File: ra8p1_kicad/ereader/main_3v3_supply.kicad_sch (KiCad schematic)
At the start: 24 parts, among them Q3 DMN2056U-7, U13 LTC3119IUFD#PBF, U16 74LVC1G17GW,125

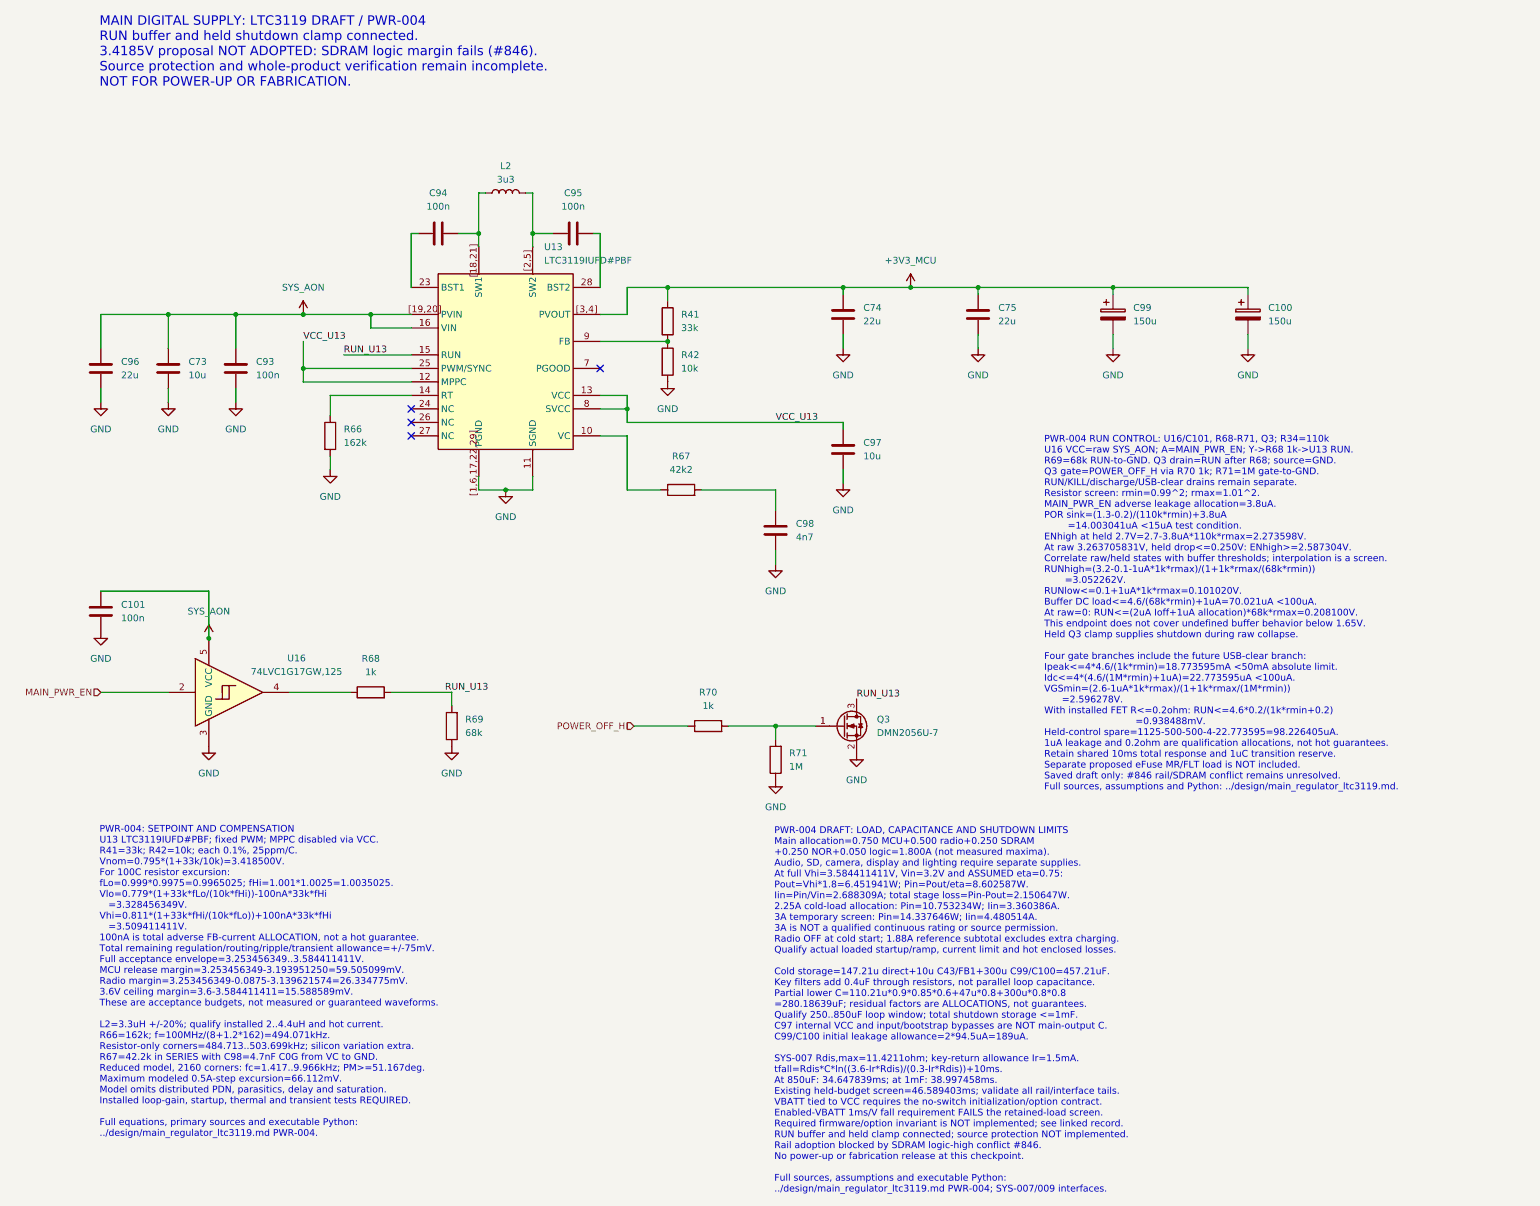
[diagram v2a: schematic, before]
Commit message: Migrate main digital supply to TPS63806 with audited calculations
Replace the LTC3119 stage in native KiCad, refresh sourced passives and linked PWR-006 calculations, and publish the full PDF and BOM. Preserve held enable control and unrelated connectivity. Reset coordination, source protection and physical qualification remain open under #825 and #846.
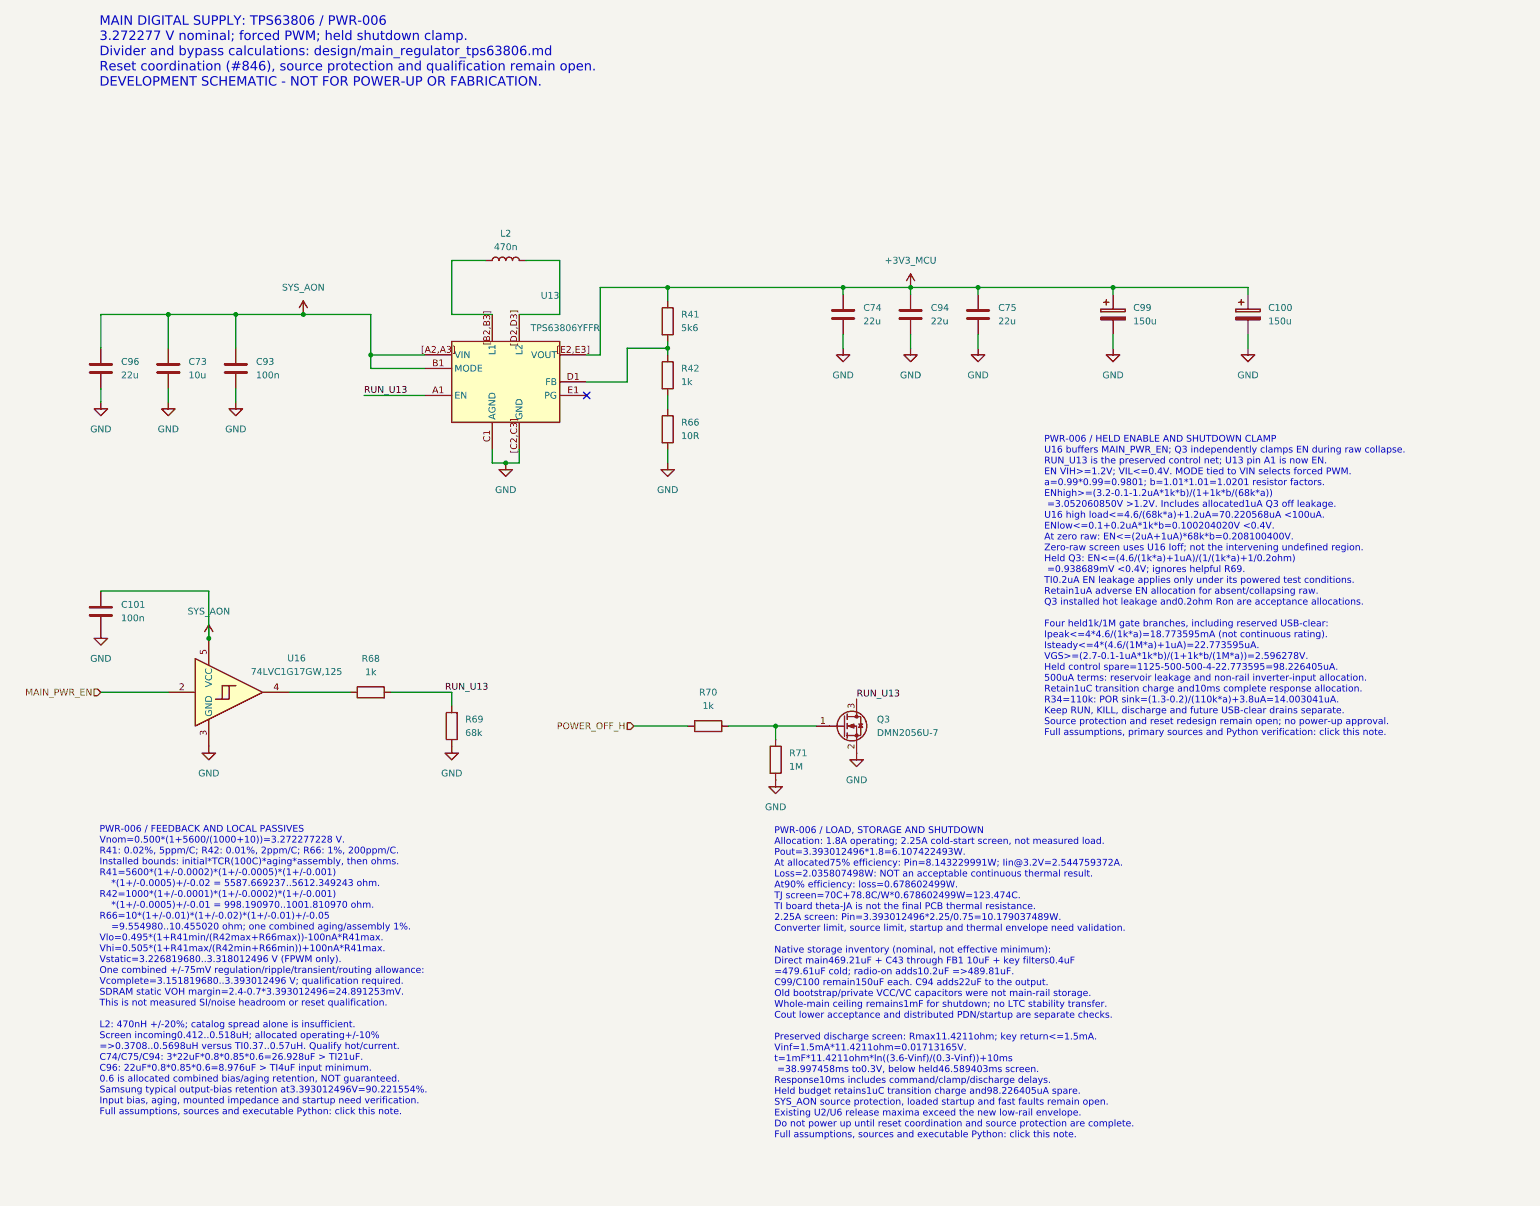
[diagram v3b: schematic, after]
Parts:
- removed C95: 100n, symbol Device:C
- removed C97: 10u, symbol Device:C
- removed C98: 4n7, symbol Device:C
- removed R67: 42k2, symbol Device:R
- removed U13: LTC3119IUFD#PBF, symbol Power_Devices:LTC3119IUFD#PBF
- added U13: TPS63806YFFR, symbol Power_Devices:TPS63806YFFR
- C74, C75: DigiKey_Part_Number 490-5890-1-ND -> 1276-3395-1-ND; DigiKey_URL https://www.digikey.com/en/products/detail/murata-electroni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 -> https://www.digikey.com/en/products/detail/samsung-electro-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; Manufacturer_Name Murata Electronics -> Samsung Electro-Mechanics; Manufacturer_Part_Number GRM32ER71C226KEA8L -> CL32B226MOJNNNE; Procurement_Status Sourced candidate; electrical qualification pending; footpr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 -> Selected; effective capacitance qualification required; foo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; Selection_Basis PWR-004: one of two retained 22uF 16V X7R 10% output cerami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 -> PWR-006: 22uF 20% 16V X7R 1210. C74/C75/C94 output; C96 inp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; Sourcing_Snapshot 2026-09-08; DigiKey stock 30854; USD qty1 0.88000; qty10 0.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 -> 2026-09-08 DigiKey: 162775 stock; USD 0.52/0.318/0.2122 at 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
- C93: Selection_Basis PWR-004: local 100nF VIN16-to-GND bypass; retain short loca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 -> PWR-006: local 100nF VIN A2/A3-to-GND bypass; not main-outp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
- C94: value 100n -> 22u; DigiKey_Part_Number 445-1314-1-ND -> 1276-3395-1-ND; DigiKey_URL https://www.digikey.com/en/products/detail/tdk-corporation/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 -> https://www.digikey.com/en/products/detail/samsung-electro-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; Manufacturer_Name TDK -> Samsung Electro-Mechanics; Manufacturer_Part_Number C1608X7R1H104K080AA -> CL32B226MOJNNNE; Procurement_Status Sourced candidate; PWR-004 installed electrical qualificati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 -> Selected; effective capacitance qualification required; foo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; Selection_Basis PWR-004: local 100nF bootstrap from BST1 pin23 to SW1 pins1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 -> PWR-006: 22uF 20% 16V X7R 1210. C74/C75/C94 output; C96 inp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; Sourcing_Snapshot 2026-09-08; DigiKey stock 372402; USD qty1 0.11000; qty10 0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 -> 2026-09-08 DigiKey: 162775 stock; USD 0.52/0.318/0.2122 at 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
- C96: DigiKey_Part_Number 490-5890-1-ND -> 1276-3395-1-ND; DigiKey_URL https://www.digikey.com/en/products/detail/murata-electroni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 -> https://www.digikey.com/en/products/detail/samsung-electro-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; Manufacturer_Name Murata Electronics -> Samsung Electro-Mechanics; Manufacturer_Part_Number GRM32ER71C226KEA8L -> CL32B226MOJNNNE; Procurement_Status Sourced candidate; electrical qualification pending; footpr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 -> Selected; effective capacitance qualification required; foo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; Selection_Basis PWR-004: 22uF PVIN-to-GND local input bypass in parallel wi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 -> PWR-006: 22uF 20% 16V X7R 1210. C74/C75/C94 output; C96 inp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; Sourcing_Snapshot 2026-09-08; DigiKey stock 30854; USD qty1 0.88000; qty10 0.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 -> 2026-09-08 DigiKey: 162775 stock; USD 0.52/0.318/0.2122 at 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
- L2: value 3u3 -> 470n; DigiKey_Part_Number 283-EXLA1V0703-3R3-RCT-ND -> 2457-XGL5020-471MEC-ND; DigiKey_URL https://www.digikey.com/en/products/detail/eaton-electronic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 -> https://www.digikey.com/en/products/detail/coilcraft/XGL502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; Manufacturer_Name Eaton -> Coilcraft; Manufacturer_Part_Number EXLA1V0703-3R3-R -> XGL5020-471MEC; Procurement_Status Sourced candidate; installed electrical and thermal qualifi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 -> Selected prototype candidate; incoming and hot/current qual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; Selection_Basis PWR-004: 3.3uH +/-20%; 18mOhm max at 25C; 10A heating and 1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 -> PWR-006: 0.47uH 20%; incoming screen 0.412..0.518uH plus al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; Sourcing_Snapshot 2026-09-08; DigiKey stock 1393; USD qty1 1.44; qty10 1.182;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 -> 2026-09-08 DigiKey Marketplace/Coilcraft: 785 available; US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
- R41: value 33k -> 5k6; DigiKey_Part_Number RG16P33.0KBCT-ND -> 408-RG2012V-562-P-T1CT-ND; DigiKey_URL https://www.digikey.com/en/products/detail/susumu/RG1608P-3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 -> https://www.digikey.com/en/products/detail/susumu/RG2012V-5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; Manufacturer_Part_Number RG1608P-333-B-T5 -> RG2012V-562-P-T1; Procurement_Status Sourced candidate; electrical qualification pending; footpr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 -> Selected; unreserved stock snapshot; footprint deferred; Selection_Basis PWR-004: upper feedback 33k 0.1% 25ppm/C; 100C excursion an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 -> PWR-006: 5k6 upper feedback; 0.02%, 5ppm/C; installed toler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; Sourcing_Snapshot 2026-09-08; DigiKey stock 18305; USD qty1 0.11; unreserved -> 2026-09-08 DigiKey cut tape: 702 stock; USD 2.18/1.808/1.50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
- R42: value 10k -> 1k; DigiKey_Part_Number YAG1236CT-ND -> 408-1631-1-ND; DigiKey_URL https://www.digikey.com/en/products/detail/yageo/RT0603BRD0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 -> https://www.digikey.com/en/products/detail/susumu/RG2012L-1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; Manufacturer_Name Yageo -> Susumu; Manufacturer_Part_Number RT0603BRD0710KL -> RG2012L-102-L-T05; Procurement_Status Sourced candidate; electrical qualification pending; footpr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 -> Selected; unreserved stock snapshot; footprint deferred; Selection_Basis PWR-004: lower feedback 10k 0.1% 25ppm/C to quiet GND, pair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 -> PWR-006: 1k lower feedback in series with R66 10R; 0.01%, 2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; Sourcing_Snapshot 2026-09-08; DigiKey stock 145267; USD qty1 0.10000; qty10 0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 -> 2026-09-08 DigiKey cut tape: 501 stock; USD 3.66/3.026/2.53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
- R66: value 162k -> 10R; DigiKey_Part_Number 13-AC0603FR-07162KLCT-ND -> 311-10.0HRCT-ND; DigiKey_URL https://www.digikey.com/en/products/detail/yageo/AC0603FR-0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 -> https://www.digikey.com/en/products/detail/yageo/RC0603FR-0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; Manufacturer_Name Yageo -> YAGEO; Manufacturer_Part_Number AC0603FR-07162KL -> RC0603FR-0710RL; Procurement_Status Sourced candidate; electrical qualification pending; footpr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 -> Selected; unreserved stock snapshot; footprint deferred; Selection_Basis PWR-004: LTC3119 RT to quiet GND; f=100MHz/(8+1.2*162)=494.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 -> PWR-006: 10R lower feedback trim in series with R42 1k; 1%,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; Sourcing_Snapshot 2026-09-08; DigiKey stock 23478; USD qty1 0.11; qty10 0.029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 -> 2026-09-08 DigiKey cut tape: 36360 stock; USD 0.10/0.037/0.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
- U16: Selection_Basis PWR-004: SYS_AON raw-powered RUN buffer with partial-power-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 -> PWR-006: SYS_AON raw-powered EN buffer with partial-power-d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
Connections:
- net +3V3_MCU: now also C94.1, U13.[E2,E3] (VOUT)
- net GND: now also C94.2, U13.C1 (AGND), U13.[C2,C3] (GND); no longer R42.2
- net RUN_U13: now also U13.A1 (EN)
- net SYS_AON: now also U13.B1 (MODE), U13.[A2,A3] (VIN)
- net at R41.2, R42.1: now also U13.D1 (FB)
- net at R66.1: now also R42.2
- net at L2.2: now also U13.[D2,D3] (L2)
- net at L2.1: now also U13.[B2,B3] (L1); no longer C94.2
- no-connect marks 4 -> 1
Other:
- note added: "MAIN DIGITAL SUPPLY: TPS63806 / PWR-006 3.272277 V nominal; forced PWM; held shutdown clamp. Divider and bypass calculations: design/main_regulator_tps63806.md Reset coordination (#846), source protection and qualification remain open. DEVELOPMENT SCHEMATIC - NOT FOR POWER-UP OR FABRICATION."
- note added: "PWR-006 / FEEDBACK AND LOCAL PASSIVES Vnom=0.500*(1+5600/(1000+10))=3.272277228 V. R41: 0.02%, 5ppm/C; R42: 0.01%, 2ppm/C; R66: 1%, 200ppm/C. Installed bounds: initial*TCR(100C)*aging*assembly, then ohms. R41=5600*(1+/-0.0002)*(1+/-0.0005)*(1+/-0.001) *(1+/-0.0005)+/-0.02 = 5587.669237..5612.349243 ohm. R42=1000*(1+/-0.0001)*(1+/-0.0002)*(1+/-0.001) *(1+/-0.0005)+/-0.01 = 998.190970..1001.810970 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"
- note added: "PWR-006 / HELD ENABLE AND SHUTDOWN CLAMP U16 buffers MAIN_PWR_EN; Q3 independently clamps EN during raw collapse. RUN_U13 is the preserved control net; U13 pin A1 is now EN. EN VIH>=1.2V; VIL<=0.4V. MODE tied to VIN selects forced PWM. a=0.99*0.99=0.9801; b=1.01*1.01=1.0201 resistor factors. ENhigh>=(3.2-0.1-1.2uA*1k*b)/(1+1k*b/(68k*a)) =3.052060850V >1.2V. Includes allocated1uA Q3 off leakage. U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"
- note added: "PWR-006 / LOAD, STORAGE AND SHUTDOWN Allocation: 1.8A operating; 2.25A cold-start screen, not measured load. Pout=3.393012496*1.8=6.107422493W. At allocated75% efficiency: Pin=8.143229991W; Iin@3.2V=2.544759372A. Loss=2.035807498W: NOT an acceptable continuous thermal result. At90% efficiency: loss=0.678602499W. TJ screen=70C+78.8C/W*0.678602499W=123.474C. TI board theta-JA is not the final PCB t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"
- note removed: "MAIN DIGITAL SUPPLY: LTC3119 DRAFT / PWR-004 RUN buffer and held shutdown clamp connected. 3.4185V proposal NOT ADOPTED: SDRAM logic margin fails (#846). Source protection and whole-product verification remain incomplete. NOT FOR POWER-UP OR FABRICATION."
- note removed: "PWR-004 DRAFT: LOAD, CAPACITANCE AND SHUTDOWN LIMITS Main allocation=0.750 MCU+0.500 radio+0.250 SDRAM +0.250 NOR+0.050 logic=1.800A (not measured maxima). Audio, SD, camera, display and lighting require separate supplies. At full Vhi=3.584411411V, Vin=3.2V and ASSUMED eta=0.75: Pout=Vhi*1.8=6.451941W; Pin=Pout/eta=8.602587W. Iin=Pin/Vin=2.688309A; total stage loss=Pin-Pout=2.150647W. 2.25A cold-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"
- note removed: "PWR-004 RUN CONTROL: U16/C101, R68-R71, Q3; R34=110k U16 VCC=raw SYS_AON; A=MAIN_PWR_EN; Y->R68 1k->U13 RUN. R69=68k RUN-to-GND. Q3 drain=RUN after R68; source=GND. Q3 gate=POWER_OFF_H via R70 1k; R71=1M gate-to-GND. RUN/KILL/discharge/USB-clear drains remain separate. Resistor screen: rmin=0.99^2; rmax=1.01^2. MAIN_PWR_EN adverse leakage allocation=3.8uA. POR sink=(1.3-0.2)/(110k*rmin)+3.8uA =14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"
- note removed: "PWR-004: SETPOINT AND COMPENSATION U13 LTC3119IUFD#PBF; fixed PWM; MPPC disabled via VCC. R41=33k; R42=10k; each 0.1%, 25ppm/C. Vnom=0.795*(1+33k/10k)=3.418500V. For 100C resistor excursion: fLo=0.999*0.9975=0.9965025; fHi=1.001*1.0025=1.0035025. Vlo=0.779*(1+33k*fLo/(10k*fHi))-100nA*33k*fHi =3.328456349V. Vhi=0.811*(1+33k*fHi/(10k*fLo))+100nA*33k*fHi =3.509411411V. 100nA is total adverse FB-curr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"
- moved on the sheet: C94, L2, R42, R66

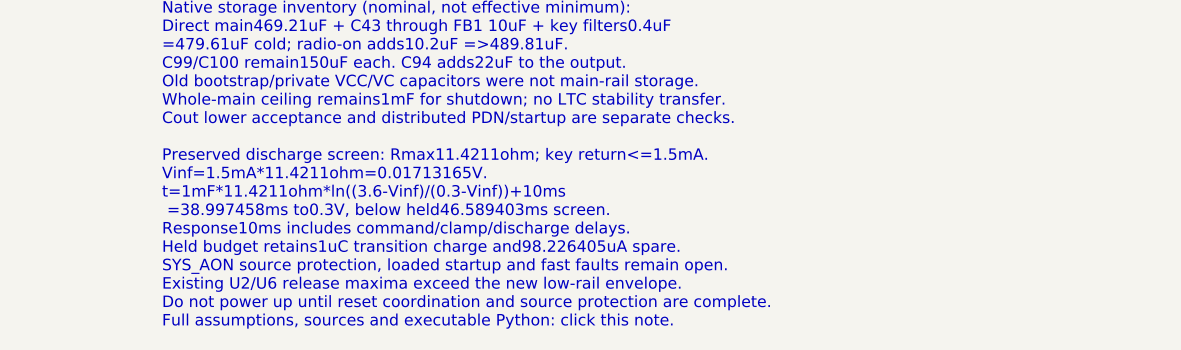
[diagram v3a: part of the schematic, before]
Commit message: hardware: migrate radio switch to TPS22964C (#826, #846)
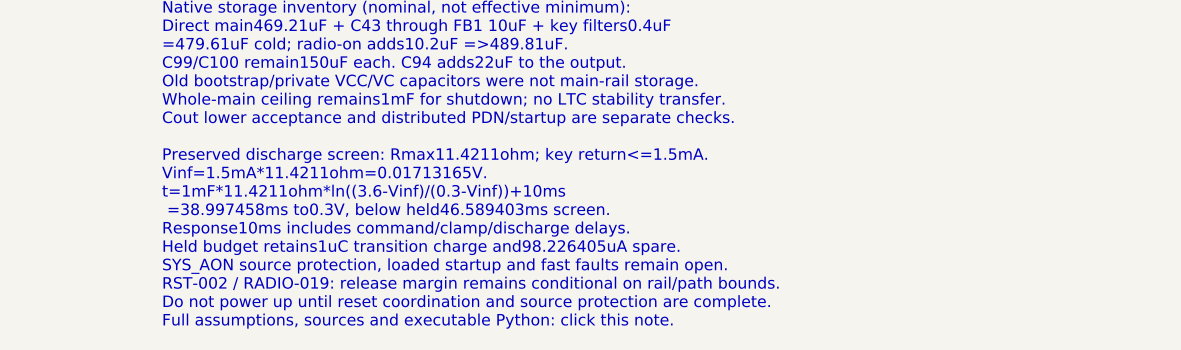
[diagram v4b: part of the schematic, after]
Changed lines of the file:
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@@
 		(rev "0.3 DRAFT")
 	)
-	(text "PWR-006 / LOAD, STORAGE AND SHUTDOWN\nAllocation: 1.8A operating; 2.25A cold-start screen, not measured load.\nPout=3.393012496*1.8=6.107422493W.\nAt allocated75% efficiency: Pin=8.143229991W; Iin@3.2V=2.544759372A.\nLoss=2.035807498W: NOT an acceptable continuous thermal result.\nAt90% efficiency: loss=0.678602499W.\nTJ screen=70C+78.8C/W*0.678602499W=123.474C.\nTI board theta-JA is not the final PCB thermal resistance.\n2.25A screen: Pin=3.393012496*2.25/0.75=10.179037489W.\nConverter limit, source limit, startup and thermal envelope need validation.\n\nNative storage inventory (nominal, not effective minimum):\nDirect main469.21uF + C43 through FB1 10uF + key filters0.4uF\n=479.61uF cold; radio-on adds10.2uF =>489.81uF.\nC99/C100 remain150uF each. C94 adds22uF to the output.\nOld bootstrap/private VCC/VC capacitors were not main-rail storage.\nWhole-main ceiling remains1mF for shutdown; no LTC stability transfer.\nCout lower acceptance and distributed PDN/startup are separate checks.\n\nPreserved discharge screen: Rmax11.4211ohm; key return<=1.5mA.\nVinf=1.5mA*11.4211ohm=0.01713165V.\nt=1mF*11.4211ohm*ln((3.6-Vinf)/(0.3-Vinf))+10ms\n =38.997458ms to0.3V, below held46.589403ms screen.\nResponse10ms includes command/clamp/discharge delays.\nHeld budget retains1uC transition charge and98.226405uA spare.\nSYS_AON source protection, loaded startup and fast faults remain open.\nExisting U2/U6 release maxima exceed the new low-rail envelope.\nDo not power up until reset coordination and source protection are complete.\nFull assumptions, sources and executable Python: click this note."
+	(text "PWR-006 / LOAD, STORAGE AND SHUTDOWN\nAllocation: 1.8A operating; 2.25A cold-start screen, not measured load.\nPout=3.393012496*1.8=6.107422493W.\nAt allocated75% efficiency: Pin=8.143229991W; Iin@3.2V=2.544759372A.\nLoss=2.035807498W: NOT an acceptable continuous thermal result.\nAt90% efficiency: loss=0.678602499W.\nTJ screen=70C+78.8C/W*0.678602499W=123.474C.\nTI board theta-JA is not the final PCB thermal resistance.\n2.25A screen: Pin=3.393012496*2.25/0.75=10.179037489W.\nConverter limit, source limit, startup and thermal envelope need validation.\n\nNative storage inventory (nominal, not effective minimum):\nDirect main469.21uF + C43 through FB1 10uF + key filters0.4uF\n=479.61uF cold; radio-on adds10.2uF =>489.81uF.\nC99/C100 remain150uF each. C94 adds22uF to the output.\nOld bootstrap/private VCC/VC capacitors were not main-rail storage.\nWhole-main ceiling remains1mF for shutdown; no LTC stability transfer.\nCout lower acceptance and distributed PDN/startup are separate checks.\n\nPreserved discharge screen: Rmax11.4211ohm; key return<=1.5mA.\nVinf=1.5mA*11.4211ohm=0.01713165V.\nt=1mF*11.4211ohm*ln((3.6-Vinf)/(0.3-Vinf))+10ms\n =38.997458ms to0.3V, below held46.589403ms screen.\nResponse10ms includes command/clamp/discharge delays.\nHeld budget retains1uC transition charge and98.226405uA spare.\nSYS_AON source protection, loaded startup and fast faults remain open.\nRST-002 / RADIO-019: release margin remains conditional on rail/path bounds.\nDo not power up until reset coordination and source protection are complete.\nFull assumptions, sources and executable Python: click this note."
 		(exclude_from_sim no)
 		(at 215.646 190.5 0)
